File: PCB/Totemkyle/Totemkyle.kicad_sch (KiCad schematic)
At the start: 88 parts, among them J1 MJ-4PP-9, J2 MJ-4PP-9, U1 xiao-ble, U2 xiao-ble

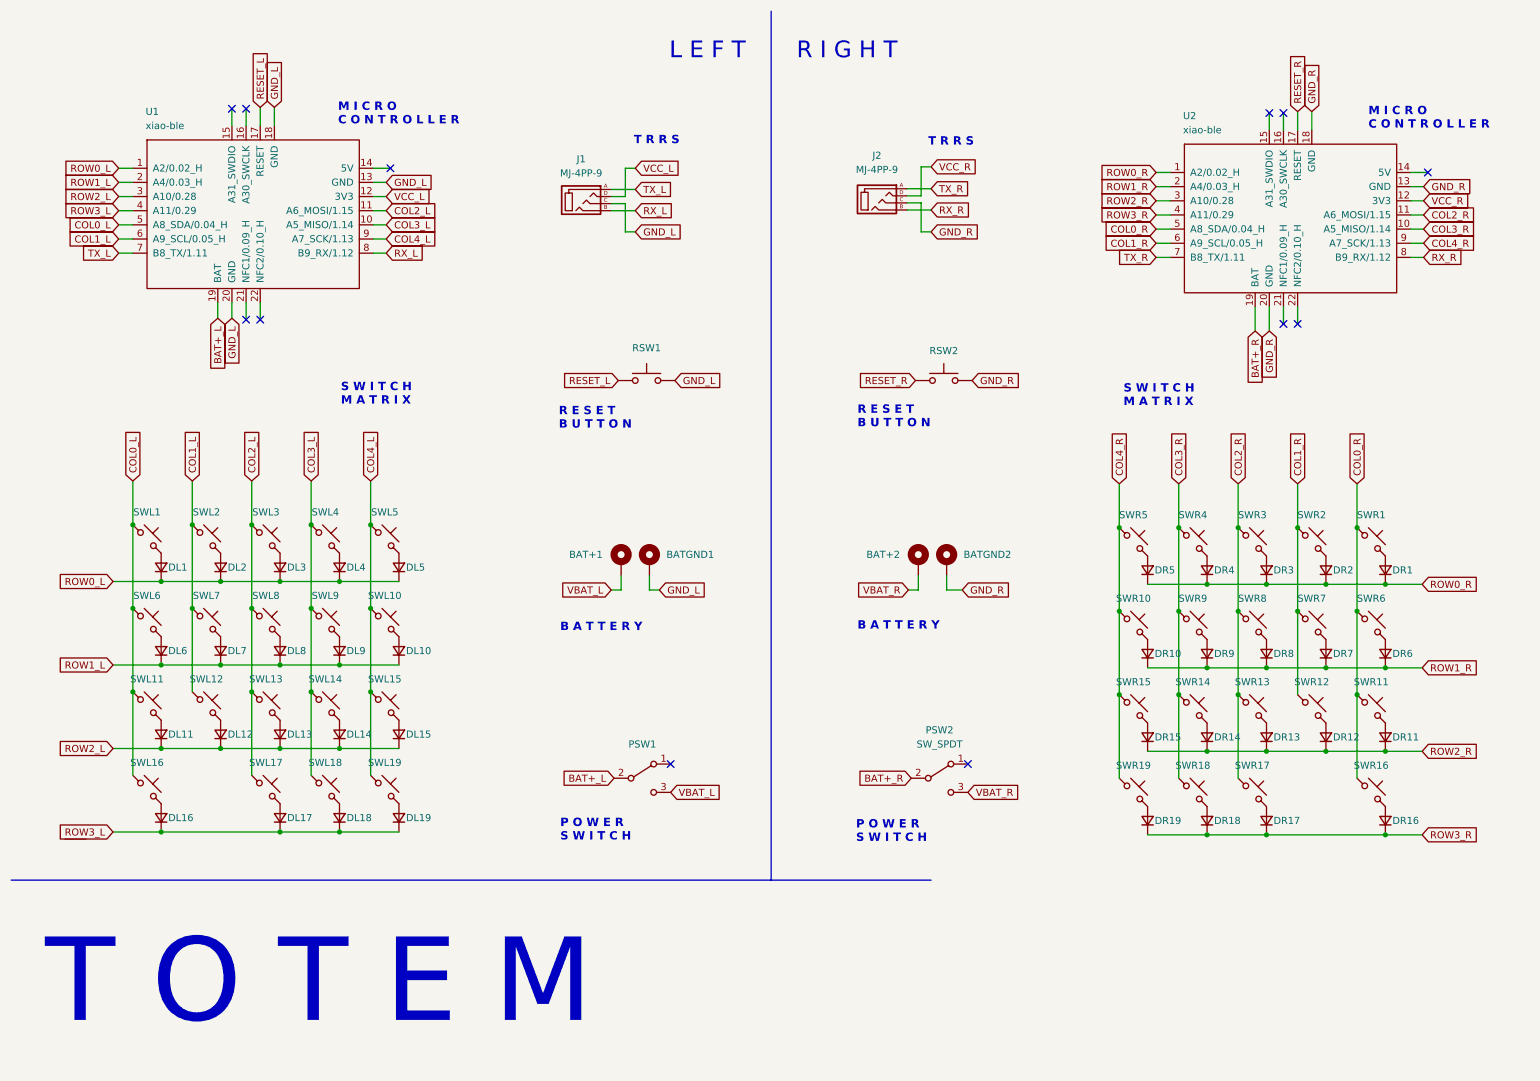
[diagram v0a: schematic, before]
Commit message: add encoder & switch
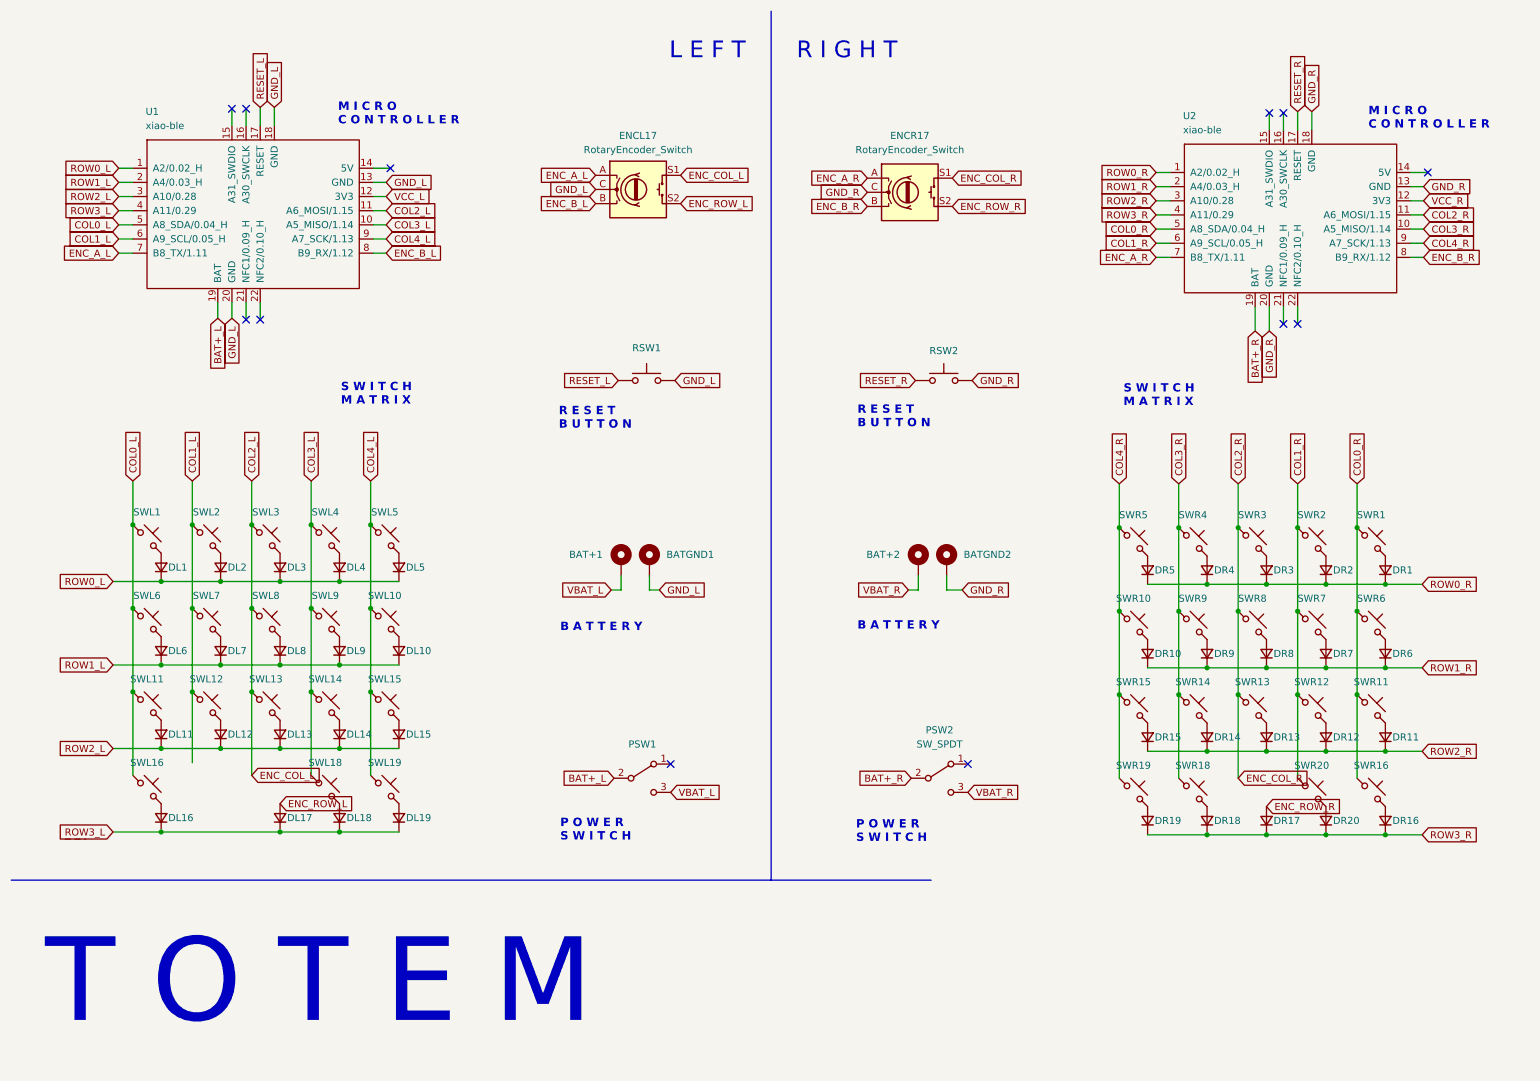
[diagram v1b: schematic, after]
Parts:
- removed J1, J2: MJ-4PP-9, TOTEMlib:MJ-4PP-9_1side, symbol kbd:MJ-4PP-9
- removed SWL17, SWR17: SW_Push_45deg, TOTEMlib:Kailh_socket_PG1350_optional, symbol Switch:SW_Push_45deg
- added DR20: D_Small, TOTEMlib:Diode_SOD123, symbol Device:D_Small
- added ENCL17: RotaryEncoder_Switch, BrownSugar_KBD:RollerEncoder+SW_horizontal, symbol Device:RotaryEncoder_Switch
- added ENCR17: RotaryEncoder_Switch, BrownSugar_KBD:RollerEncoder_SW_Vertical, symbol Device:RotaryEncoder_Switch
- added SWR20: SW_Push_45deg, TOTEMlib:Kailh_socket_PG1350, symbol Switch:SW_Push_45deg
- SWL1, SWL10, SWL11, SWL12, SWL13, SWL14, SWL15, SWL16, SWL18, SWL19, SWL2, SWL3, SWL4, SWL5, SWL6, SWL7, SWL8, SWL9, SWR1, SWR10, SWR11, SWR12, SWR13, SWR14, SWR15, SWR16, SWR18, SWR19, SWR2, SWR3, SWR4, SWR5, SWR6, SWR7, SWR8, SWR9: footprint TOTEMlib:Kailh_socket_PG1350_optional -> TOTEMlib:Kailh_socket_PG1350
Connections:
- net COL1_R: now also SWR20.1
- net COL2_L: now also ENCL17.S1
- net COL2_R: now also ENCR17.S1
- net GND_L: now also ENCL17.C
- net GND_R: now also ENCR17.C
- net ROW3_R: now also DR20.1 (K)
- net ENC_ROW_L: now reaches DL17.2 (A)
- net ENC_ROW_L: now also ENCL17.S2
- net ENC_ROW_R: now reaches DR17.2 (A)
- net ENC_ROW_R: now also ENCR17.S2
- net RX_L renamed ENC_B_L
- net ENC_B_L: now also ENCL17.B
- net RX_R renamed ENC_B_R
- net ENC_B_R: now also ENCR17.B
- net TX_L renamed ENC_A_L
- net ENC_A_L: now also ENCL17.A
- net TX_R renamed ENC_A_R
- net ENC_A_R: now also ENCR17.A
- new net: DR20.2 (A), SWR20.2
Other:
- note removed: "T R R S"
